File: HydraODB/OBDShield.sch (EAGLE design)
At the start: 23 parts, among them CN1 8p-2.54, J1 HYDRABUS_SHIELD_CON_HEADER_2X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, J2 HYDRABUS_SHIELD_CON_HEADER_2X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, J3 HYDRABUS_SHIELD_CON_HEADER_2X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, K1 TS-1188E, U1 SN65HVD233DG4, U2 SN65HVD233DG4, U3 CJ78M05-to252

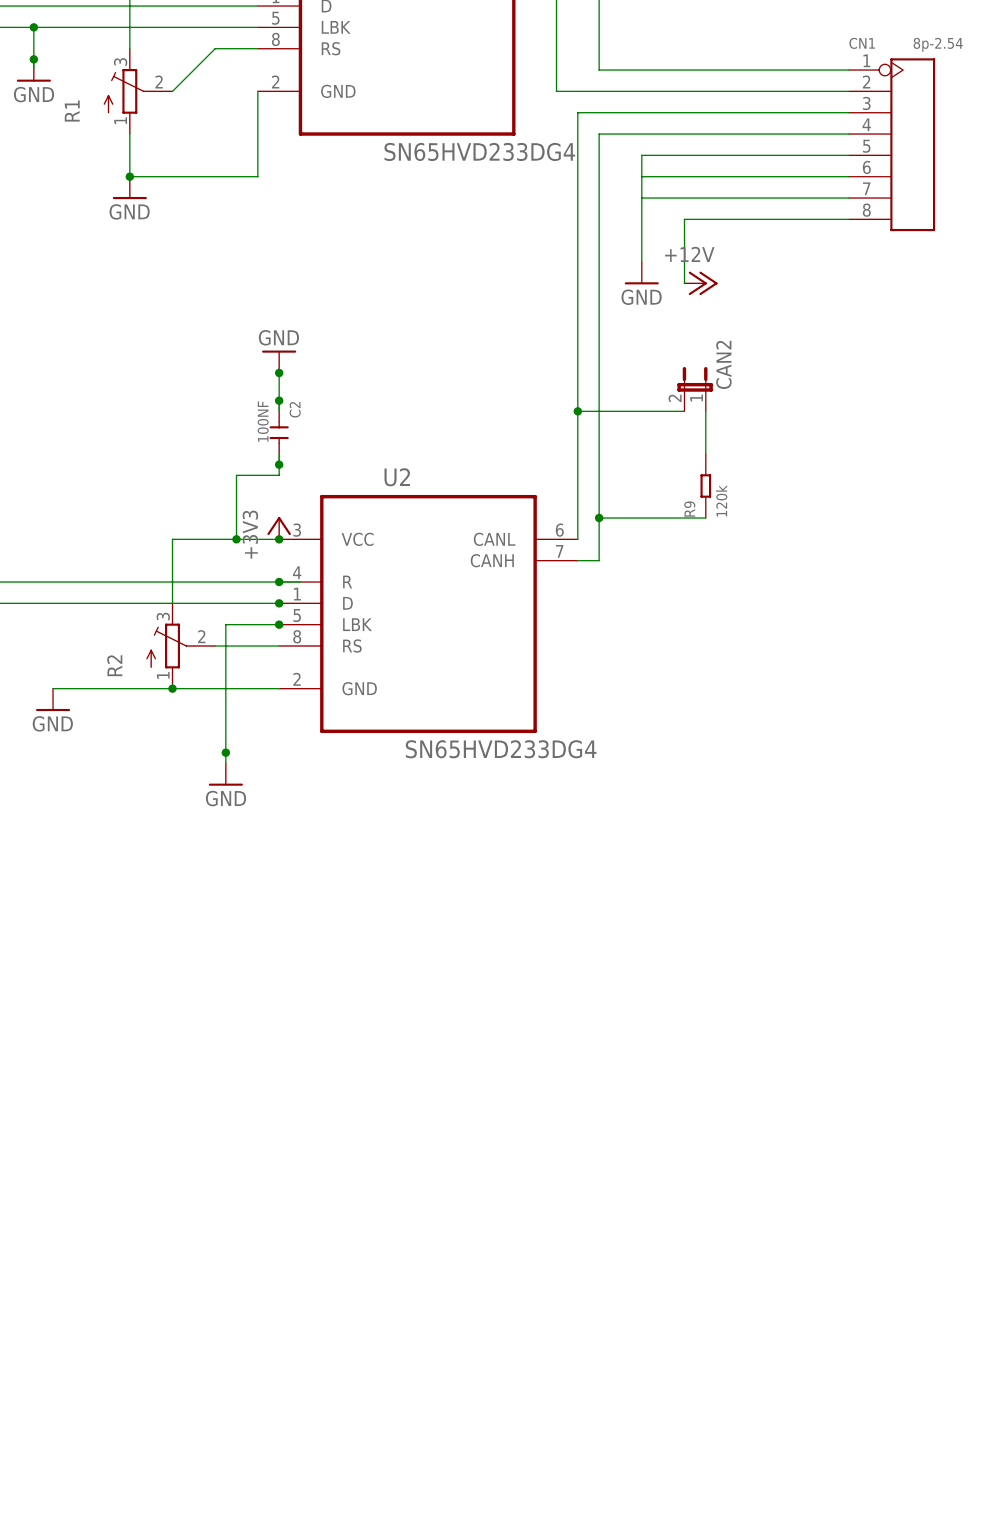
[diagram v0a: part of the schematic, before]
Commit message: Added 2 LIN Bus transceivers
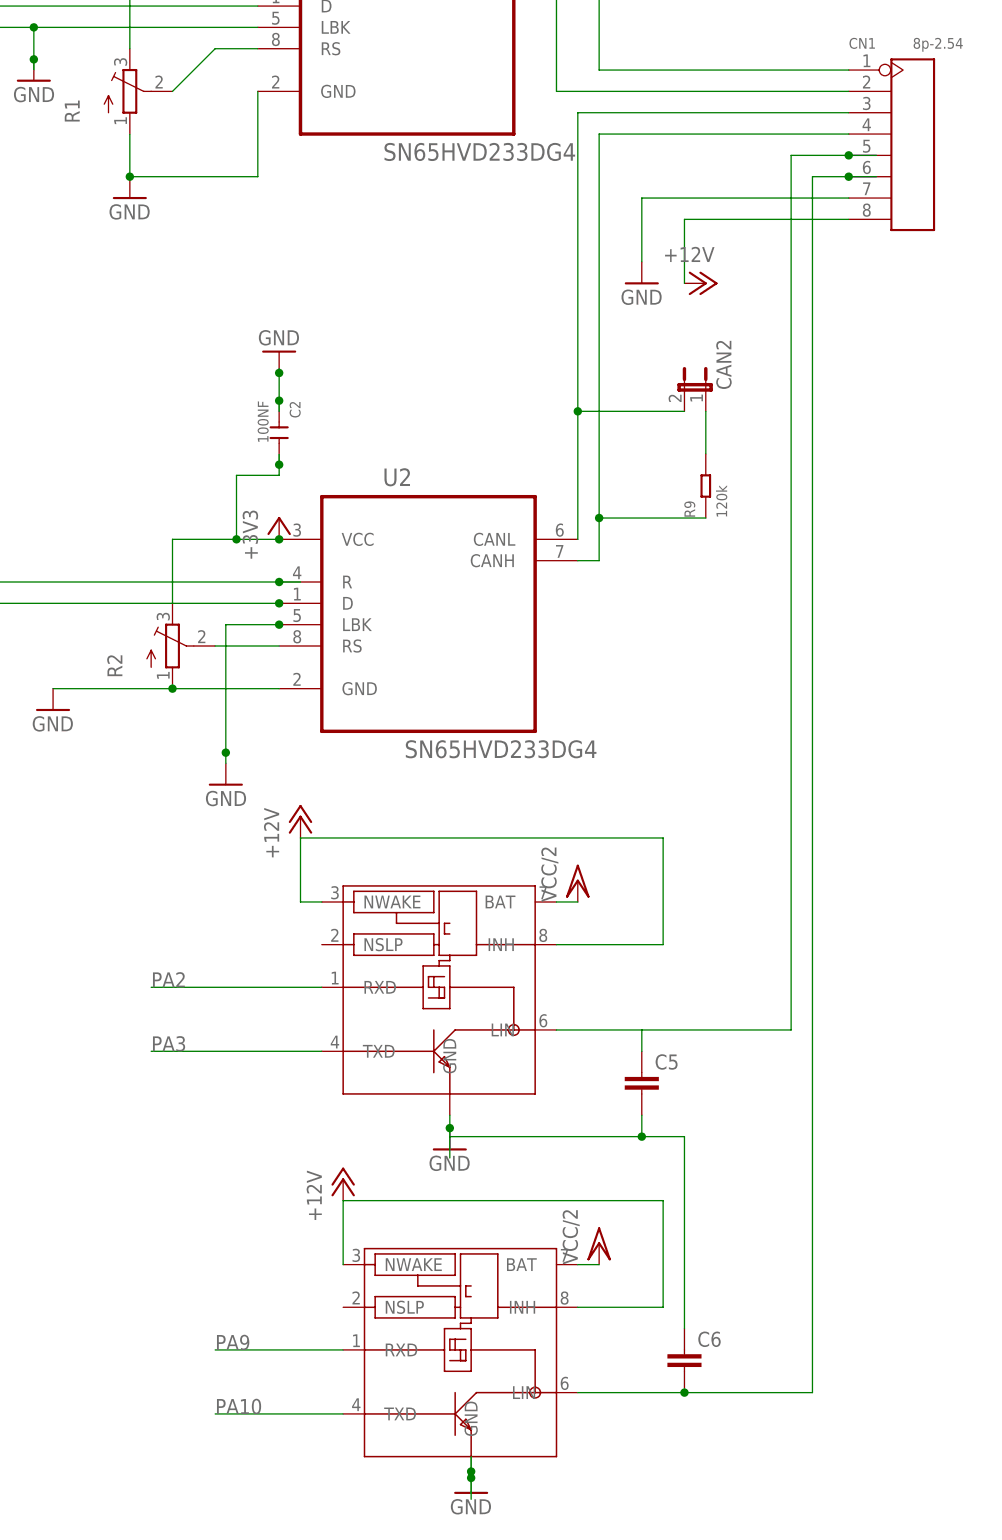
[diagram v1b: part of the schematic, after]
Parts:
- added C5, C6: (no value), _c2h:CAP1206
- added U$1, U$2: TJA1020SO8, nxp:TJA1020SO8
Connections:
- new net N$4: C5.1, CN1.5, U$1.LIN
- new net N$7: C6.2, CN1.6, U$2.LIN
- net +12V: now also U$1.INH, U$1.NWAKE, U$2.INH, U$2.NWAKE
- net GND: now also C5.2, C6.1, U$1.GND, U$2.GND; no longer CN1.5, CN1.6
- net PA10: now also U$2.TXD
- net PA2: now also U$1.RXD
- net PA3: now also U$1.TXD
- net PA9: now also U$2.RXD
- net VCC/2: now also U$1.BAT, U$2.BAT
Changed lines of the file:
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@@
 <?xml version="1.0" encoding="utf-8"?>
 <!DOCTYPE eagle SYSTEM "eagle.dtd">
-<eagle version="7.5.0">
+<eagle version="8.1.0">
 <drawing>
 <settings>
@@
 <layer number="56" name="wert" color="7" fill="1" visible="no" active="no"/>
 <layer number="57" name="tCAD" color="7" fill="1" visible="no" active="no"/>
+<layer number="59" name="tCarbon" color="7" fill="1" visible="no" active="no"/>
+<layer number="60" name="bCarbon" color="7" fill="1" visible="no" active="no"/>
 <layer number="90" name="Modules" color="5" fill="1" visible="yes" active="yes"/>
 <layer number="91" name="Nets" color="2" fill="1" visible="yes" active="yes"/>
@@
 <part name="TC1" library="testpad" deviceset="TP" device="B2,54"/>
 <part name="CN1" library="Seeed-OPL-Connector" deviceset="DIP-BLACK-FEMALE-HEADER-VERT(8P-2.54)" device="" value="8p-2.54"/>
+<part name="U$1" library="nxp" deviceset="TJA1020" device="SO8"/>
+<part name="U$2" library="nxp" deviceset="TJA1020" device="SO8"/>
+<part name="GND1" library="supply1" deviceset="GND" device=""/>
+<part name="GND4" library="supply1" deviceset="GND" device=""/>
+<part name="P+5" library="supply1" deviceset="VCC/2" device=""/>
+<part name="P+6" library="supply1" deviceset="VCC/2" device=""/>
+<part name="P+8" library="supply1" deviceset="+12V" device=""/>
+<part name="P+9" library="supply1" deviceset="+12V" device=""/>
+<part name="C5" library="_c2h" deviceset="CAP" device="1206"/>
+<part name="C6" library="_c2h" deviceset="CAP" device="1206"/>
 </parts>
 <sheets>
@@
 <instance part="TC1" gate="G$1" x="124.46" y="99.06" rot="R180"/>
 <instance part="CN1" gate="G$1" x="235.458" y="90.17"/>
+<instance part="U$1" gate="G$1" x="172.72" y="-7.62"/>
+<instance part="U$2" gate="G$1" x="175.26" y="-50.8"/>
+<instance part="GND1" gate="1" x="180.34" y="-29.464"/>
+<instance part="GND4" gate="1" x="182.88" y="-70.358"/>
+<instance part="P+5" gate="G$1" x="195.58" y="2.54"/>
+<instance part="P+6" gate="G$1" x="198.12" y="-40.64"/>
+<instance part="P+8" gate="1" x="162.56" y="10.16"/>
+<instance part="P+9" gate="1" x="167.64" y="-33.02"/>
+<instance part="C5" gate="G$1" x="203.2" y="-22.86"/>
+<instance part="C6" gate="G$1" x="208.28" y="-55.88"/>
 </instances>
 <busses>
@@
 <pinref part="GND8" gate="1" pin="GND"/>
 <wire x1="203.2" y1="76.2" x2="203.2" y2="83.82" width="0.1524" layer="91"/>
-<wire x1="203.2" y1="83.82" x2="203.2" y2="86.36" width="0.1524" layer="91"/>
-<wire x1="203.2" y1="86.36" x2="203.2" y2="88.9" width="0.1524" layer="91"/>
 <wire x1="203.2" y1="83.82" x2="227.838" y2="83.82" width="0.1524" layer="91"/>
-<wire x1="203.2" y1="86.36" x2="227.838" y2="86.36" width="0.1524" layer="91"/>
-<wire x1="203.2" y1="88.9" x2="227.838" y2="88.9" width="0.1524" layer="91"/>
-<pinref part="CN1" gate="G$1" pin="5"/>
-<pinref part="CN1" gate="G$1" pin="6"/>
 <pinref part="CN1" gate="G$1" pin="7"/>
 </segment>
@@
 <junction x="160.02" y="62.992"/>
 </segment>
+<segment>
+<pinref part="U$1" gate="G$1" pin="GND"/>
+<wire x1="180.34" y1="-25.4" x2="180.34" y2="-26.924" width="0.1524" layer="91"/>
+<pinref part="GND1" gate="1" pin="GND"/>
+<wire x1="180.34" y1="-26.924" x2="180.34" y2="-27.94" width="0.1524" layer="91"/>
+<junction x="180.34" y="-26.924"/>
+<pinref part="C5" gate="G$1" pin="2"/>
+<wire x1="180.34" y1="-27.94" x2="180.34" y2="-30.48" width="0.1524" layer="91"/>
+<wire x1="180.34" y1="-27.94" x2="203.2" y2="-27.94" width="0.1524" layer="91"/>
+<wire x1="203.2" y1="-27.94" x2="203.2" y2="-25.4" width="0.1524" layer="91"/>
+<pinref part="C6" gate="G$1" pin="1"/>
+<wire x1="203.2" y1="-27.94" x2="208.28" y2="-27.94" width="0.1524" layer="91"/>
+<wire x1="208.28" y1="-27.94" x2="208.28" y2="-50.8" width="0.1524" layer="91"/>
+<junction x="203.2" y="-27.94"/>
+</segment>
+<segment>
+<wire x1="182.88" y1="-71.12" x2="182.88" y2="-68.58" width="0.1524" layer="91"/>
+<pinref part="GND4" gate="1" pin="GND"/>
+<wire x1="182.88" y1="-68.58" x2="182.88" y2="-67.818" width="0.1524" layer="91"/>
+<wire x1="182.88" y1="-67.818" x2="182.88" y2="-66.04" width="0.1524" layer="91"/>
+<junction x="182.88" y="-67.818"/>
+<pinref part="U$2" gate="G$1" pin="GND"/>
+<junction x="182.88" y="-68.58"/>
+</segment>
 </net>
 <net name="USB0D_P" class="0">
@@
 <pinref part="J2" gate="J" pin="14"/>
 </segment>
+<segment>
+<pinref part="U$2" gate="G$1" pin="TXD"/>
+<wire x1="167.64" y1="-60.96" x2="152.4" y2="-60.96" width="0.1524" layer="91"/>
+<label x="152.4" y="-60.96" size="1.778" layer="95"/>
+</segment>
 </net>
 <net name="PA9" class="0">
@@
 <label x="25.654" y="109.22" size="1.778" layer="95"/>
 <pinref part="J2" gate="J" pin="16"/>
+</segment>
+<segment>
+<pinref part="U$2" gate="G$1" pin="RXD"/>
+<wire x1="167.64" y1="-53.34" x2="152.4" y2="-53.34" width="0.1524" layer="91"/>
+<label x="152.4" y="-53.34" size="1.778" layer="95"/>
 </segment>
 </net>
@@
 <pinref part="J2" gate="J" pin="9"/>
 </segment>
+<segment>
+<pinref part="U$1" gate="G$1" pin="TXD"/>
+<wire x1="165.1" y1="-17.78" x2="144.78" y2="-17.78" width="0.1524" layer="91"/>
+<label x="144.78" y="-17.78" size="1.778" layer="95"/>
+</segment>
 </net>
 <net name="PA2" class="0">
@@
 <label x="0" y="119.38" size="1.778" layer="95"/>
 <pinref part="J2" gate="J" pin="7"/>
+</segment>
+<segment>
+<pinref part="U$1" gate="G$1" pin="RXD"/>
+<wire x1="165.1" y1="-10.16" x2="144.78" y2="-10.16" width="0.1524" layer="91"/>
+<label x="144.78" y="-10.16" size="1.778" layer="95"/>
 </segment>
 </net>
@@
 <wire x1="208.28" y1="81.28" x2="227.838" y2="81.28" width="0.1524" layer="91"/>
 <pinref part="CN1" gate="G$1" pin="8"/>
+</segment>
+<segment>
+<pinref part="U$1" gate="G$1" pin="NWAKE"/>
+<pinref part="P+8" gate="1" pin="+12V"/>
+<wire x1="165.1" y1="0" x2="162.56" y2="0" width="0.1524" layer="91"/>
+<wire x1="162.56" y1="0" x2="162.56" y2="7.62" width="0.1524" layer="91"/>
+<wire x1="162.56" y1="7.62" x2="205.74" y2="7.62" width="0.1524" layer="91"/>
+<wire x1="205.74" y1="7.62" x2="205.74" y2="-5.08" width="0.1524" layer="91"/>
+<pinref part="U$1" gate="G$1" pin="INH"/>
+<wire x1="205.74" y1="-5.08" x2="193.04" y2="-5.08" width="0.1524" layer="91"/>
+</segment>
+<segment>
+<pinref part="U$2" gate="G$1" pin="NWAKE"/>
+<pinref part="P+9" gate="1" pin="+12V"/>
+<wire x1="167.64" y1="-43.18" x2="167.64" y2="-35.56" width="0.1524" layer="91"/>
+<wire x1="167.64" y1="-35.56" x2="205.74" y2="-35.56" width="0.1524" layer="91"/>
+<wire x1="205.74" y1="-35.56" x2="205.74" y2="-48.26" width="0.1524" layer="91"/>
+<pinref part="U$2" gate="G$1" pin="INH"/>
+<wire x1="205.74" y1="-48.26" x2="195.58" y2="-48.26" width="0.1524" layer="91"/>
 </segment>
 </net>
@@
 <wire x1="20.32" y1="91.44" x2="25.4" y2="91.44" width="0.1524" layer="91"/>
 </segment>
+<segment>
+<pinref part="U$1" gate="G$1" pin="BAT"/>
+<pinref part="P+5" gate="G$1" pin="VCC/2"/>
+<wire x1="193.04" y1="0" x2="195.58" y2="0" width="0.1524" layer="91"/>
+</segment>
+<segment>
+<pinref part="U$2" gate="G$1" pin="BAT"/>
+<pinref part="P+6" gate="G$1" pin="VCC/2"/>
+<wire x1="198.12" y1="-43.18" x2="195.58" y2="-43.18" width="0.1524" layer="91"/>
+</segment>
 </net>
 <net name="N$6" class="2">
@@
 </segment>
 </net>
+<net name="N$4" class="0">
+<segment>
+<pinref part="U$1" gate="G$1" pin="LIN"/>
+<wire x1="193.04" y1="-15.24" x2="203.2" y2="-15.24" width="0.1524" layer="91"/>
+<wire x1="203.2" y1="-15.24" x2="220.98" y2="-15.24" width="0.1524" layer="91"/>
+<wire x1="220.98" y1="-15.24" x2="220.98" y2="88.9" width="0.1524" layer="91"/>
+<wire x1="220.98" y1="88.9" x2="227.838" y2="88.9" width="0.1524" layer="91"/>
+<pinref part="C5" gate="G$1" pin="1"/>
+<wire x1="227.838" y1="88.9" x2="231.14" y2="88.9" width="0.1524" layer="91"/>
+<wire x1="203.2" y1="-17.78" x2="203.2" y2="-15.24" width="0.1524" layer="91"/>
+<pinref part="CN1" gate="G$1" pin="5"/>
+<junction x="227.838" y="88.9"/>
+</segment>
+</net>
+<net name="N$7" class="0">
+<segment>
+<pinref part="U$2" gate="G$1" pin="LIN"/>
+<wire x1="195.58" y1="-58.42" x2="208.28" y2="-58.42" width="0.1524" layer="91"/>
+<wire x1="208.28" y1="-58.42" x2="223.52" y2="-58.42" width="0.1524" layer="91"/>
+<wire x1="223.52" y1="-58.42" x2="223.52" y2="86.36" width="0.1524" layer="91"/>
+<wire x1="223.52" y1="86.36" x2="227.838" y2="86.36" width="0.1524" layer="91"/>
+<pinref part="C6" gate="G$1" pin="2"/>
+<junction x="208.28" y="-58.42"/>
+<pinref part="CN1" gate="G$1" pin="6"/>
+<wire x1="227.838" y1="86.36" x2="231.14" y2="86.36" width="0.1524" layer="91"/>
+<junction x="227.838" y="86.36"/>
+</segment>
+</net>

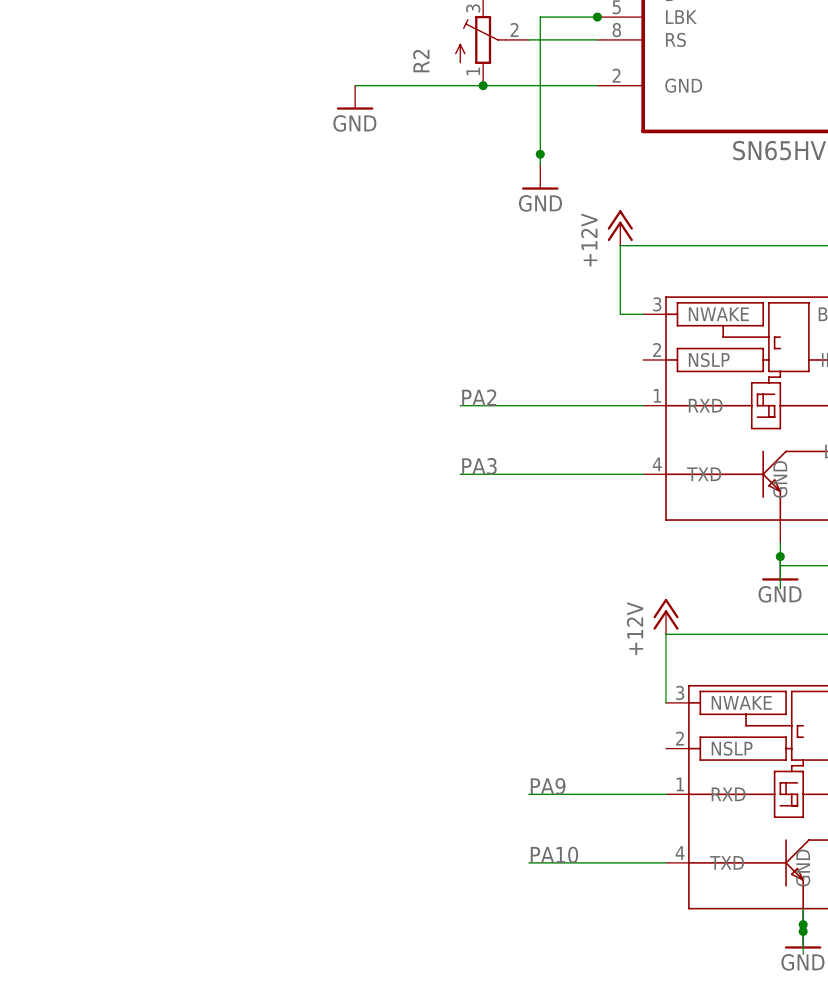
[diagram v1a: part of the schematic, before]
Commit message: Pullups for LIN transceivers
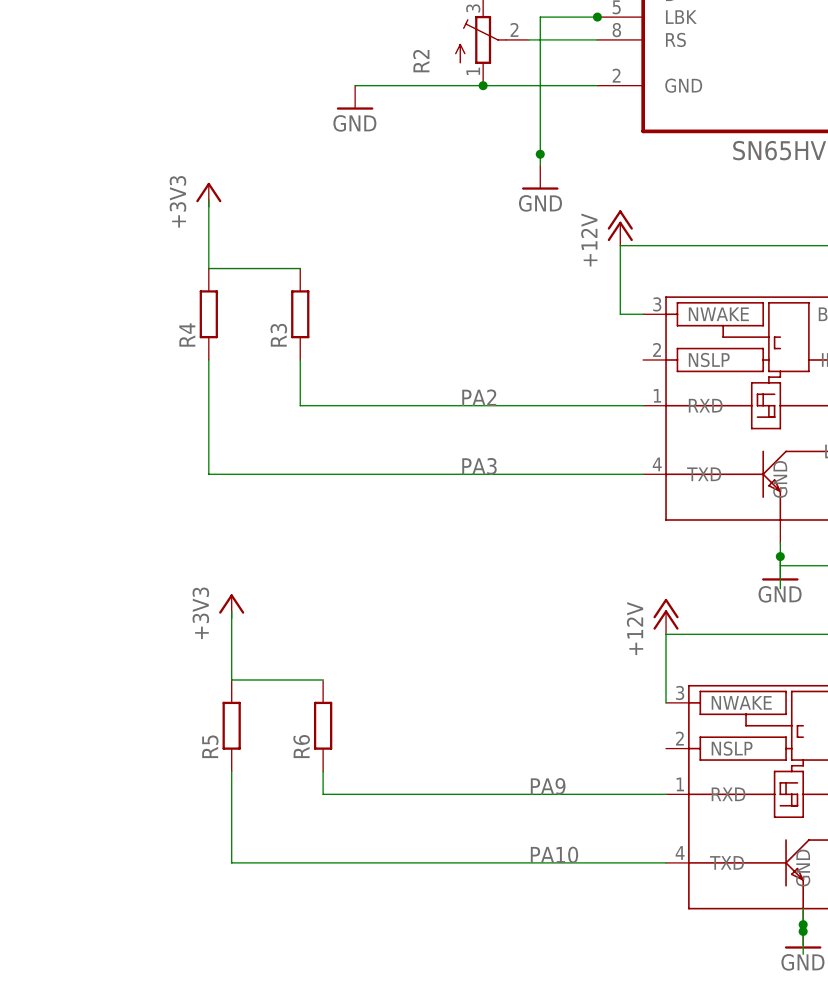
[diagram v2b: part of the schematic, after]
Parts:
- added R3, R4, R5, R6: (no value), resistor:R-EU_M1206
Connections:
- new net N$13: R3.2, R4.2
- new net N$18: R6.2
- net PA10: now also R5.1
- net PA2: now also R3.1
- net PA3: now also R4.1
- net PA9: now also R6.1
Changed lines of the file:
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@@
 <part name="C5" library="_c2h" deviceset="CAP" device="1206"/>
 <part name="C6" library="_c2h" deviceset="CAP" device="1206"/>
+<part name="R3" library="resistor" deviceset="R-EU_" device="M1206"/>
+<part name="R4" library="resistor" deviceset="R-EU_" device="M1206"/>
+<part name="R5" library="resistor" deviceset="R-EU_" device="M1206"/>
+<part name="R6" library="resistor" deviceset="R-EU_" device="M1206"/>
+<part name="+3V4" library="supply1" deviceset="+3V3" device=""/>
+<part name="+3V7" library="supply1" deviceset="+3V3" device=""/>
 </parts>
 <sheets>
@@
 <instance part="C5" gate="G$1" x="203.2" y="-22.86"/>
 <instance part="C6" gate="G$1" x="208.28" y="-55.88"/>
+<instance part="R3" gate="G$1" x="127" y="0" rot="R90"/>
+<instance part="R4" gate="G$1" x="116.84" y="0" rot="R90"/>
+<instance part="R5" gate="G$1" x="119.38" y="-45.72" rot="R90"/>
+<instance part="R6" gate="G$1" x="129.54" y="-45.72" rot="R90"/>
+<instance part="+3V4" gate="G$1" x="116.84" y="14.478"/>
+<instance part="+3V7" gate="G$1" x="119.38" y="-31.242"/>
 </instances>
 <busses>
@@
 <segment>
 <pinref part="U$2" gate="G$1" pin="TXD"/>
-<wire x1="167.64" y1="-60.96" x2="152.4" y2="-60.96" width="0.1524" layer="91"/>
 <label x="152.4" y="-60.96" size="1.778" layer="95"/>
+<pinref part="R5" gate="G$1" pin="1"/>
+<wire x1="119.38" y1="-50.8" x2="119.38" y2="-60.96" width="0.1524" layer="91"/>
+<wire x1="119.38" y1="-60.96" x2="167.64" y2="-60.96" width="0.1524" layer="91"/>
 </segment>
 </net>
@@
 <segment>
 <pinref part="U$2" gate="G$1" pin="RXD"/>
-<wire x1="167.64" y1="-53.34" x2="152.4" y2="-53.34" width="0.1524" layer="91"/>
 <label x="152.4" y="-53.34" size="1.778" layer="95"/>
+<pinref part="R6" gate="G$1" pin="1"/>
+<wire x1="129.54" y1="-50.8" x2="129.54" y2="-53.34" width="0.1524" layer="91"/>
+<wire x1="129.54" y1="-53.34" x2="167.64" y2="-53.34" width="0.1524" layer="91"/>
 </segment>
 </net>
@@
 <segment>
 <pinref part="U$1" gate="G$1" pin="TXD"/>
-<wire x1="165.1" y1="-17.78" x2="144.78" y2="-17.78" width="0.1524" layer="91"/>
 <label x="144.78" y="-17.78" size="1.778" layer="95"/>
+<pinref part="R4" gate="G$1" pin="1"/>
+<wire x1="116.84" y1="-5.08" x2="116.84" y2="-17.78" width="0.1524" layer="91"/>
+<wire x1="116.84" y1="-17.78" x2="165.1" y2="-17.78" width="0.1524" layer="91"/>
 </segment>
 </net>
@@
 <segment>
 <pinref part="U$1" gate="G$1" pin="RXD"/>
-<wire x1="165.1" y1="-10.16" x2="144.78" y2="-10.16" width="0.1524" layer="91"/>
+<wire x1="165.1" y1="-10.16" x2="127" y2="-10.16" width="0.1524" layer="91"/>
 <label x="144.78" y="-10.16" size="1.778" layer="95"/>
+<pinref part="R3" gate="G$1" pin="1"/>
+<wire x1="127" y1="-10.16" x2="127" y2="-5.08" width="0.1524" layer="91"/>
 </segment>
 </net>
@@
 </segment>
 </net>
+<net name="N$13" class="0">
+<segment>
+<pinref part="R4" gate="G$1" pin="2"/>
+<wire x1="116.84" y1="12.7" x2="116.84" y2="5.08" width="0.1524" layer="91"/>
+<pinref part="R3" gate="G$1" pin="2"/>
+<wire x1="116.84" y1="5.08" x2="127" y2="5.08" width="0.1524" layer="91"/>
+</segment>
+</net>
+<net name="N$18" class="0">
+<segment>
+<pinref part="R6" gate="G$1" pin="2"/>
+<wire x1="119.38" y1="-33.02" x2="119.38" y2="-40.64" width="0.1524" layer="91"/>
+<wire x1="119.38" y1="-40.64" x2="129.54" y2="-40.64" width="0.1524" layer="91"/>
+</segment>
+</net>
